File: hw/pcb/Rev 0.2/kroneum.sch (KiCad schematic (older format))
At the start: 18 parts, among them J1 USB_B_Micro, J2 SWD_I2C_BOOT, SW1 Boot_Mode_Btn, SW2 Ctrl_One_Btn, SW3 Reset_Btn, SW4 Ctrl_Ten_Btn, U1 STM32F042F4Px

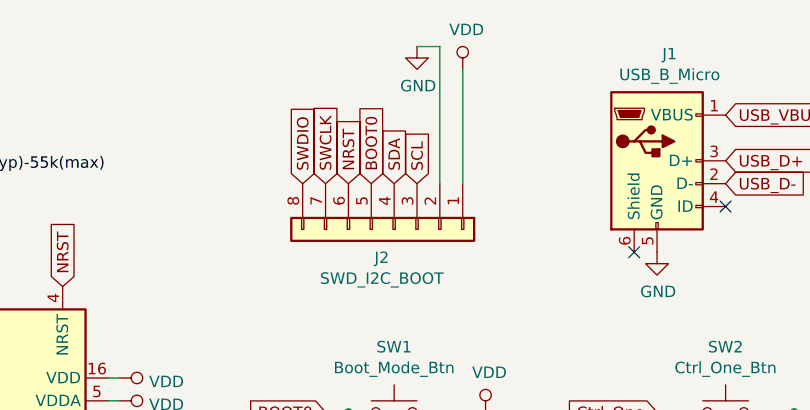
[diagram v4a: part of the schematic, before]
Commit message: hw: first PCB version with all nets connected.
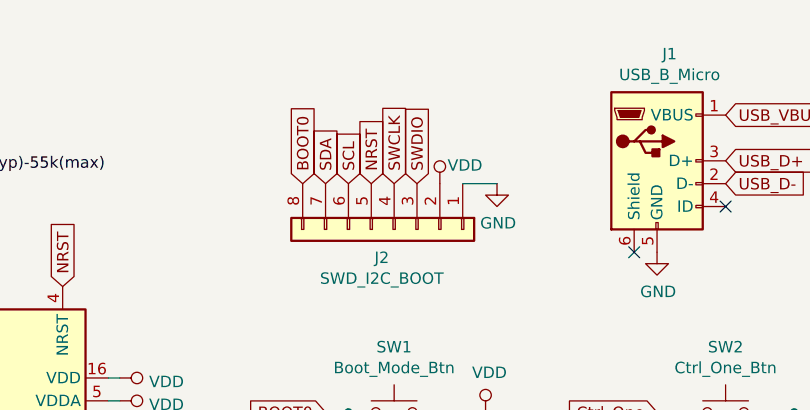
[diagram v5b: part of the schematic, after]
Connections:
- net BOOT0: now also J2.8 (Pin_8); no longer J2.5 (Pin_5)
- net GND: now also J2.1 (Pin_1); no longer J2.2 (Pin_2)
- net NRST: now also J2.5 (Pin_5); no longer J2.6 (Pin_6)
- net SCL: now also J2.6 (Pin_6); no longer J2.3 (Pin_3)
- net SDA: now also J2.7 (Pin_7); no longer J2.4 (Pin_4)
- net SWCLK: now also J2.4 (Pin_4); no longer J2.7 (Pin_7)
- net SWDIO: now also J2.3 (Pin_3); no longer J2.8 (Pin_8)
- net VDD: now also J2.2 (Pin_2); no longer J2.1 (Pin_1)
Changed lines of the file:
@@
 Text GLabel 2300 2850 1    50   Input ~ 0
 SCL
+Text GLabel 4450 2400 1    50   Input ~ 0
+NRST
+Text GLabel 4550 2400 1    50   Input ~ 0
+SWCLK
+Text GLabel 4650 2400 1    50   Input ~ 0
+SWDIO
 Text GLabel 4350 2400 1    50   Input ~ 0
-NRST
+SCL
 Text GLabel 4250 2400 1    50   Input ~ 0
-SWCLK
-Text GLabel 4150 2400 1    50   Input ~ 0
-SWDIO
-Text GLabel 4650 2400 1    50   Input ~ 0
-SCL
-Text GLabel 4550 2400 1    50   Input ~ 0
 SDA
-Wire Wire Line
-	4750 2400 4750 1800
 $Comp
 L power:GND #PWR05
 U 1 1 5C4A8CEA
-P 4650 1800
-F 0 "#PWR05" H 4650 1550 50  0001 C CNN
-F 1 "GND" H 4655 1627 50  0000 C CNN
-F 2 "" H 4650 1800 50  0001 C CNN
-F 3 "" H 4650 1800 50  0001 C CNN
-	1    4650 1800
+P 5000 2400
+F 0 "#PWR05" H 5000 2150 50  0001 C CNN
+F 1 "GND" H 5005 2227 50  0000 C CNN
+F 2 "" H 5000 2400 50  0001 C CNN
+F 3 "" H 5000 2400 50  0001 C CNN
+	1    5000 2400
 	1    0    0    -1
 $EndComp
@@
 L power:VDD #PWR04
 U 1 1 5C4A93B8
-P 4850 1900
-F 0 "#PWR04" H 4850 1750 50  0001 C CNN
-F 1 "VDD" H 4867 2073 50  0000 C CNN
-F 2 "" H 4850 1900 50  0001 C CNN
-F 3 "" H 4850 1900 50  0001 C CNN
-	1    4850 1900
+P 4750 2400
+F 0 "#PWR04" H 4750 2250 50  0001 C CNN
+F 1 "VDD" H 4860 2480 50  0000 C CNN
+F 2 "" H 4750 2400 50  0001 C CNN
+F 3 "" H 4750 2400 50  0001 C CNN
+	1    4750 2400
 	1    0    0    -1
 $EndComp
-Wire Wire Line
-	4850 1900 4850 2400
-Wire Wire Line
-	4650 1800 4750 1800
 $Comp
 L Connector_Generic:Conn_01x08 J2
@@
 	0    1    1    0
 $EndComp
-Text GLabel 4450 2400 1    50   Input ~ 0
+Text GLabel 4150 2400 1    50   Input ~ 0
 BOOT0
+Wire Wire Line
+	4850 2400 5000 2400
 $EndSCHEMATC

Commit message: hw: decrease width of TSSOP20 pads, first export of Gerbers.
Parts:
- U1: footprint Package_SO:TSSOP-20_4.4x6.5mm_P0.65mm -> tssop-20x6.5mmx4:TSSOP-20_4.4x6.5mm_P0.65mm
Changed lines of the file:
@@
 F 0 "U1" V 2600 3400 50  0000 R CNN
 F 1 "STM32F042F4Px" V 2500 3650 50  0000 R CNN
-F 2 "Package_SO:TSSOP-20_4.4x6.5mm_P0.65mm" H 2100 2750 50  0001 R CNN
+F 2 "tssop-20x6.5mmx4:TSSOP-20_4.4x6.5mm_P0.65mm" H 2100 2750 50  0001 R CNN
 F 3 "http://www.st.com/st-web-ui/static/active/en/resource/technical/document/datasheet/DM00105814.pdf" H 2600 3450 50  0001 C CNN
 	1    2600 3450

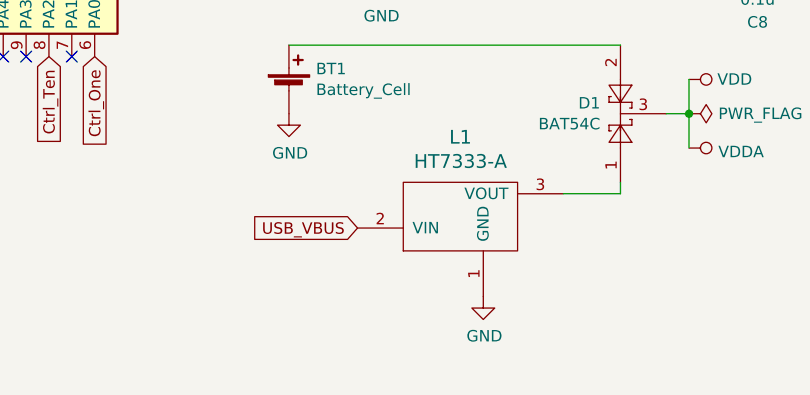
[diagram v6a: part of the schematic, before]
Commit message: hw: add decoupling capacitors for the voltage regulator.
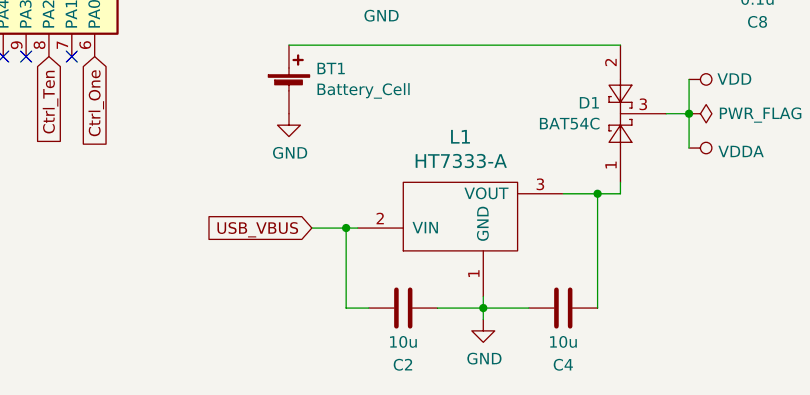
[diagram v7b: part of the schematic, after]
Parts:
- added C2, C4: 10u, Capacitor_SMD:C_0805_2012Metric_Pad1.15x1.40mm_HandSolder, symbol Device:C
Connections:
- net GND: now also C2.1, C4.2
- net USB_VBUS: now also C2.2
- net at D1.1, L1.3 (VOUT): now also C4.1
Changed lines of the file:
@@
 L power:GND #PWR0101
 U 1 1 5C229126
-P 4800 5100
-F 0 "#PWR0101" H 4800 4850 50  0001 C CNN
-F 1 "GND" H 4805 4927 50  0000 C CNN
-F 2 "" H 4800 5100 50  0001 C CNN
-F 3 "" H 4800 5100 50  0001 C CNN
-	1    4800 5100
-	1    0    0    -1
-$EndComp
-Text GLabel 4250 4800 0    50   Input ~ 0
+P 4800 5200
+F 0 "#PWR0101" H 4800 4950 50  0001 C CNN
+F 1 "GND" H 4805 5027 50  0000 C CNN
+F 2 "" H 4800 5200 50  0001 C CNN
+F 3 "" H 4800 5200 50  0001 C CNN
+	1    4800 5200
+	1    0    0    -1
+$EndComp
+Text GLabel 4050 4800 0    50   Input ~ 0
 USB_VBUS
 $Comp
@@
 Wire Wire Line
 	5700 4150 5700 4300
-Wire Wire Line
-	5150 4650 5400 4650
 Wire Wire Line
 	5400 4650 5400 4600
@@
 Wire Wire Line
 	4850 2400 5000 2400
+$Comp
+L Device:C C2
+U 1 1 5C561B67
+P 4450 5150
+F 0 "C2" V 4700 5150 50  0000 C CNN
+F 1 "10u" V 4600 5150 50  0000 C CNN
+F 2 "Capacitor_SMD:C_0805_2012Metric_Pad1.15x1.40mm_HandSolder" H 4488 5000 50  0001 C CNN
+F 3 "~" H 4450 5150 50  0001 C CNN
+	1    4450 5150
+	0    1    1    0
+$EndComp
+$Comp
+L Device:C C4
+U 1 1 5C563CA4
+P 5150 5150
+F 0 "C4" V 5400 5150 50  0000 C CNN
+F 1 "10u" V 5300 5150 50  0000 C CNN
+F 2 "Capacitor_SMD:C_0805_2012Metric_Pad1.15x1.40mm_HandSolder" H 5188 5000 50  0001 C CNN
+F 3 "~" H 5150 5150 50  0001 C CNN
+	1    5150 5150
+	0    1    1    0
+$EndComp
+Wire Wire Line
+	5150 4650 5300 4650
+Connection ~ 5300 4650
+Wire Wire Line
+	5300 4650 5400 4650
+Wire Wire Line
+	4050 4800 4200 4800
+Connection ~ 4200 4800
+Wire Wire Line
+	4200 4800 4250 4800
+Wire Wire Line
+	4200 5150 4300 5150
+Wire Wire Line
+	4200 4800 4200 5150
+Wire Wire Line
+	5300 4650 5300 5150
+Wire Wire Line
+	4800 5100 4800 5150
+Wire Wire Line
+	4600 5150 4800 5150
+Connection ~ 4800 5150
+Wire Wire Line
+	4800 5150 4800 5200
+Wire Wire Line
+	4800 5150 5000 5150
 $EndSCHEMATC
